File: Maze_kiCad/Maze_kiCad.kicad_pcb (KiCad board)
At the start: 2 copper layers, 1 part, among them U1 ESP32-S2-DevKitC-1

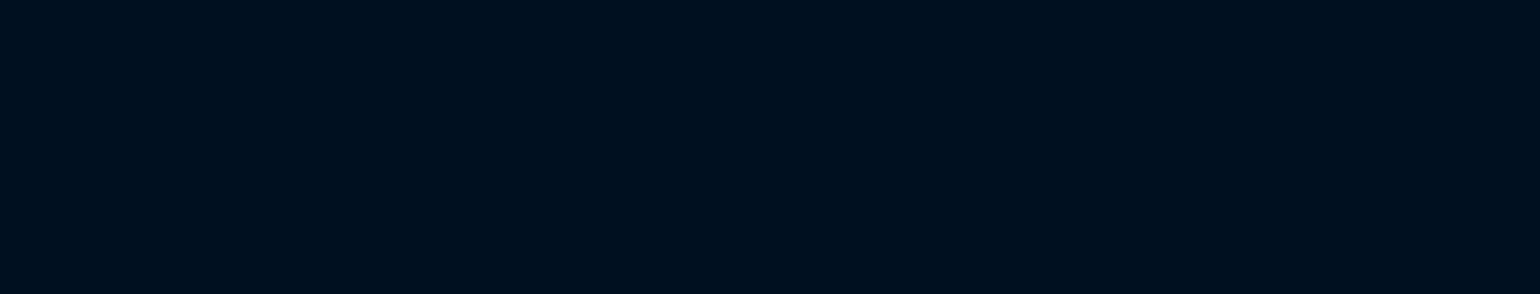
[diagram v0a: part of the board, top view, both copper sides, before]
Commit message: Add ir sensor
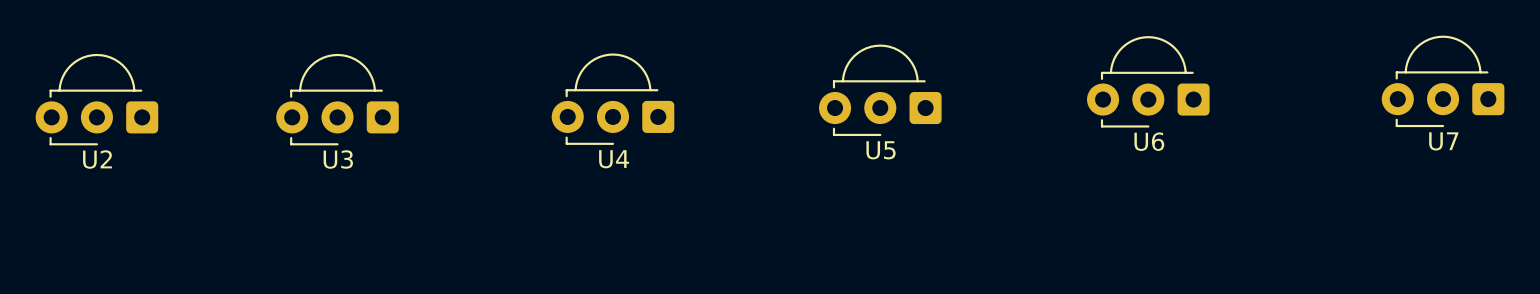
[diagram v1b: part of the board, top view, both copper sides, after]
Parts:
- added U2: TSSP58038, OptoDevice:Vishay_MINICAST-3Pin, F.Cu at (105.5, 27.0)
- added U3: TSSP58038, OptoDevice:Vishay_MINICAST-3Pin, F.Cu at (119.0, 27.0)
- added U4: TSSP58038, OptoDevice:Vishay_MINICAST-3Pin, F.Cu at (134.5, 27.0)
- added U5: TSSP58038, OptoDevice:Vishay_MINICAST-3Pin, F.Cu at (149.5, 26.5)
- added U6: TSSP58038, OptoDevice:Vishay_MINICAST-3Pin, F.Cu at (164.5, 26.0)
- added U7: TSSP58038, OptoDevice:Vishay_MINICAST-3Pin, F.Cu at (181.1, 26.0)

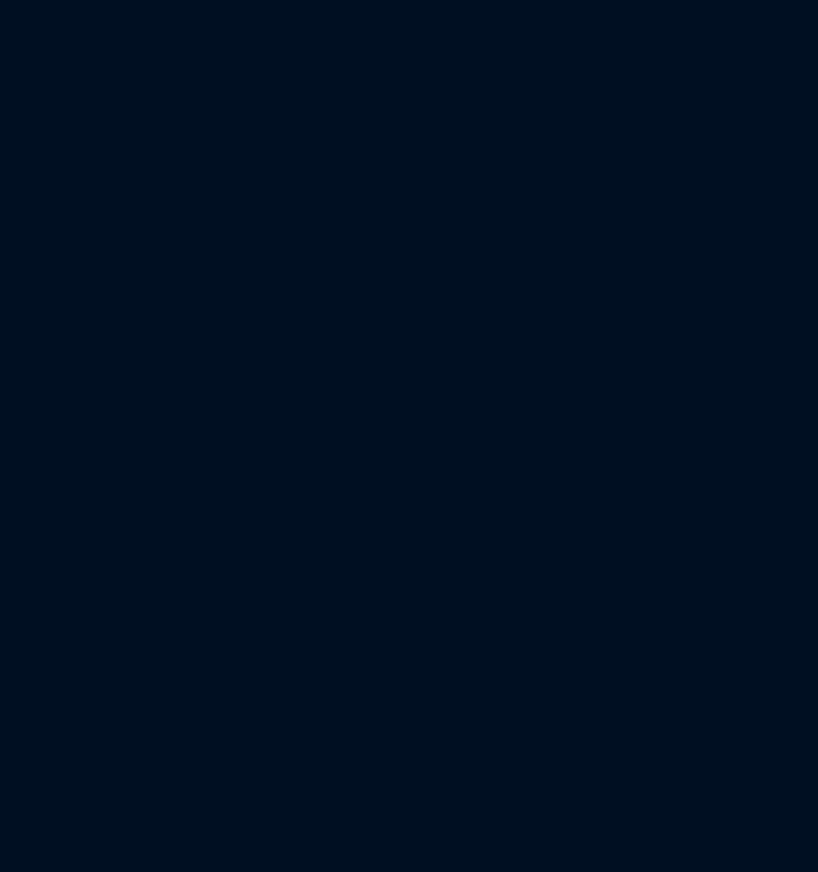
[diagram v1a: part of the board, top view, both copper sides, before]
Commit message: add gyroscope symbol-footprint
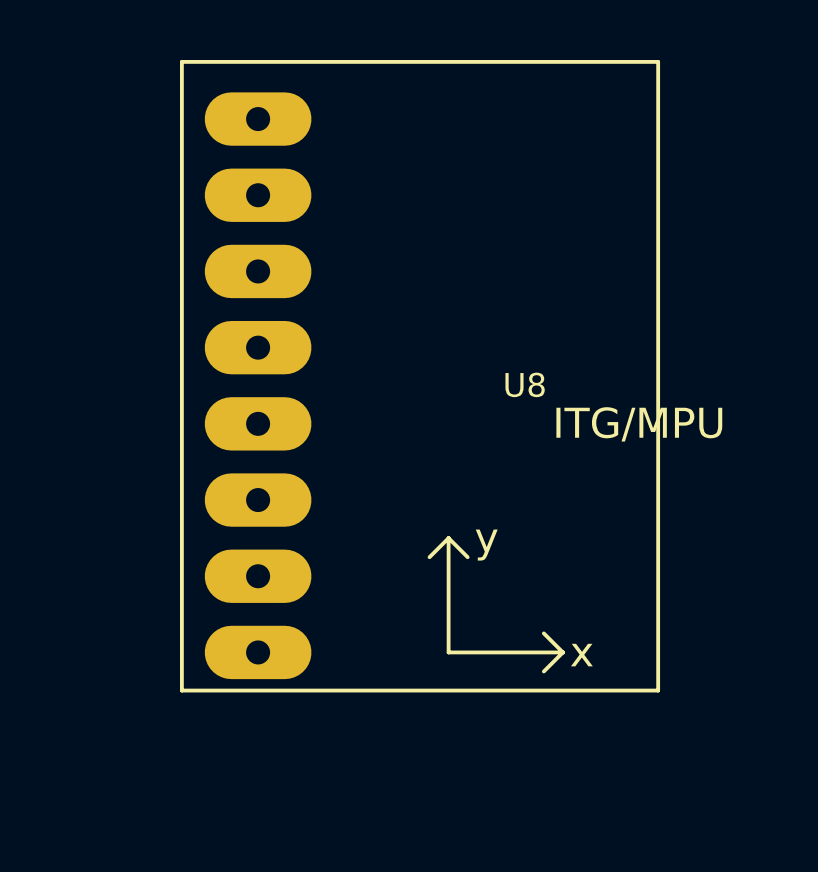
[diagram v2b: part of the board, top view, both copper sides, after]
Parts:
- added U8: GY-521, mpu6050:GY-521, F.Cu at (226.0, 30.5)

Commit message: drv8835 motor driver symnol and footprint
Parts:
- added MotorDriver1: DRV8835, drv8835:drv8835, F.Cu at (75.0, 35.0)

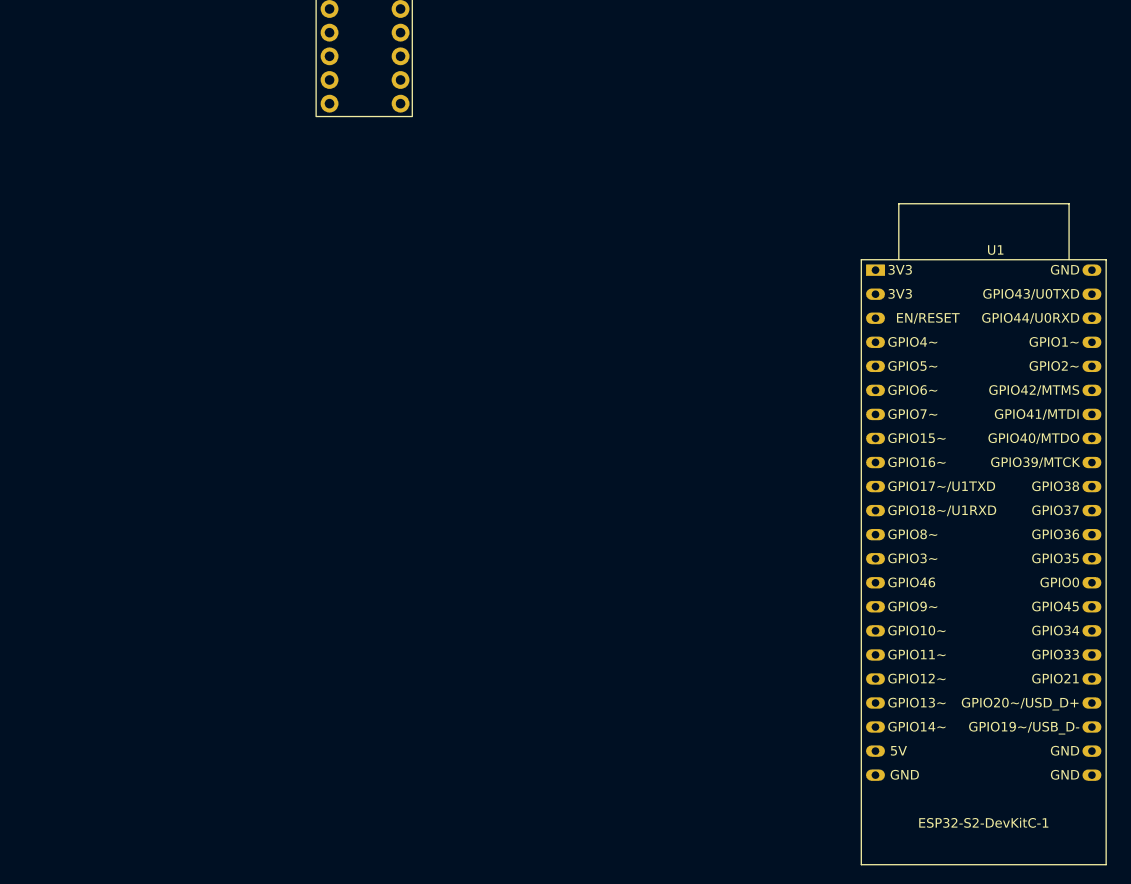
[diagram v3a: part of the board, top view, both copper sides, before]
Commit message: add ultra sonic symbol and footprint
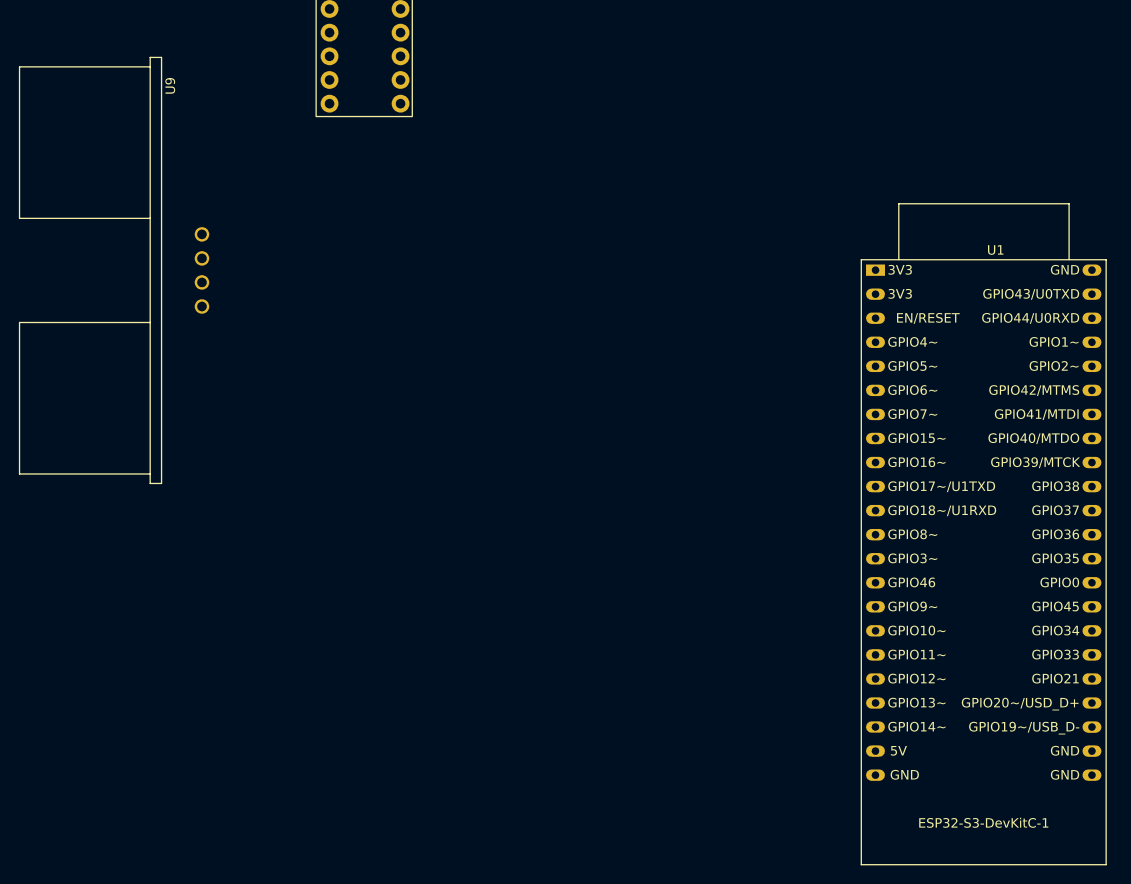
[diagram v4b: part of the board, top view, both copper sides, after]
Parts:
- added U9: HC-SR04, ultrasonic:XCVR_HC-SR04, F.Cu at (58.0, 60.2)
- U1: value ESP32-S2-DevKitC-1 -> ESP32-S3-DevKitC-1
- U2, U3, U4, U5, U6, U7: value TSSP58038 -> TCRT5000
- U8: value GY-521 -> Gyro mpu-6050

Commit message: assign footprints
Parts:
- added D1: RGB, LED_THT:LED_D5.0mm-4_RGB_Staggered_Pins, F.Cu at (112.1, 148.7)
- added D2: RGB, LED_THT:LED_D5.0mm-4_RGB_Staggered_Pins, F.Cu at (112.2, 164.5)
- added J1: Screw_Terminal, TerminalBlock_Phoenix:TerminalBlock_Phoenix_MPT-0,5-2-2.54_1x02_P2.54mm_Horizontal, F.Cu at (109.0, 123.0)
- added J10: pins: 42_41_40_39_38_37, Connector_PinSocket_2.54mm:PinSocket_1x06_P2.54mm_Vertical, F.Cu at (80.0, 100.3)
- added J11: pins: 42_41_40_39_38_37, Connector_PinSocket_2.54mm:PinSocket_1x06_P2.54mm_Vertical, F.Cu at (89.5, 116.2)
- added J12: Vcc/Gnd, Connector_PinSocket_2.54mm:PinSocket_1x04_P2.54mm_Vertical, F.Cu at (131.4, 153.0)
- added J2: motor2, Connector_PinSocket_2.54mm:PinSocket_1x02_P2.54mm_Vertical, F.Cu at (93.0, 93.5)
- added J3: motor1, Connector_PinSocket_2.54mm:PinSocket_1x02_P2.54mm_Vertical, F.Cu at (93.5, 82.8)
- added J4: Vmm/Mode, Connector_PinSocket_2.54mm:PinSocket_1x02_P2.54mm_Vertical, F.Cu at (105.5, 68.0)
- added J5: INT/ADO/XCL/XDA, Connector_PinSocket_2.54mm:PinSocket_1x04_P2.54mm_Vertical, F.Cu at (25.0, 47.0)
- added J6: GND, Connector_PinSocket_2.54mm:PinSocket_1x01_P2.54mm_Vertical, F.Cu at (212.0, 41.5)
- added J7: IR Receiver, Connector_PinSocket_2.54mm:PinSocket_1x03_P2.54mm_Vertical, F.Cu at (121.5, 86.5)
- added J8: pins: 5v/12_11_10_9_46, Connector_PinSocket_2.54mm:PinSocket_1x06_P2.54mm_Vertical, F.Cu at (24.0, 137.0)
- added J9: pins: 3.3v/RST/43_44_2, Connector_PinSocket_2.54mm:PinSocket_1x06_P2.54mm_Vertical, F.Cu at (42.5, 66.5)
- added R1: 220-ohm, Resistor_THT:R_Axial_DIN0204_L3.6mm_D1.6mm_P7.62mm_Horizontal, F.Cu at (84.2, 139.0)
- added R2: 220-ohm, Resistor_THT:R_Axial_DIN0204_L3.6mm_D1.6mm_P7.62mm_Horizontal, F.Cu at (93.7, 150.5)
- added R3: 220-ohm, Resistor_THT:R_Axial_DIN0204_L3.6mm_D1.6mm_P7.62mm_Horizontal, F.Cu at (92.2, 158.0)
- added R4: 220-ohm, Resistor_THT:R_Axial_DIN0204_L3.6mm_D1.6mm_P7.62mm_Horizontal, F.Cu at (96.9, 168.0)
- added R5: 220-ohm, Resistor_THT:R_Axial_DIN0204_L3.6mm_D1.6mm_P7.62mm_Horizontal, F.Cu at (62.9, 163.5)
- added R6: 220-ohm, Resistor_THT:R_Axial_DIN0204_L3.6mm_D1.6mm_P7.62mm_Horizontal, F.Cu at (90.7, 187.0)
- added S1: RB141C1100, RB141C1100:SW_RB141C1100, F.Cu at (134.0, 119.0)
- added U10: Reg S7V7F5, Connector_PinSocket_2.54mm:PinSocket_1x03_P2.54mm_Vertical, F.Cu at (104.4, 107.5)
- moved U8 182.2 mm to (44.0, 38.5)
- moved U9 145.3 mm to (202.0, 40.9), turned to 180 degrees
- moved U1 95.1 mm to (38.6, 89.3)
- moved U7 71.1 mm to (110.0, 23.5)
- moved MotorDriver1 60.0 mm to (106.5, 86.1), turned to 180 degrees
- moved U2 40.2 mm to (145.5, 23.5)
- moved U5 22.2 mm to (171.5, 23.5)
- moved U3 15.4 mm to (134.0, 23.5)
- moved U4 13.5 mm to (121.5, 23.5)
- moved U6 6.50 mm to (158.5, 23.5)
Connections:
- U1 pad 1: unconnected-(U1-3V3-Pad1) -> Net-(J9-Pin_3)
- U1 pad 10: unconnected-(U1-GPIO17/ADC2_CH6/U1TXD-Pad10) -> /ir_sensor_4
- U1 pad 11: unconnected-(U1-GPIO18/ADC2_CH7/U1RXD-Pad11) -> /ir_sensor_3
- U1 pad 12: unconnected-(U1-GPIO8/ADC1_CH7-Pad12) -> /ir_sensor_2
- U1 pad 13: unconnected-(U1-GPIO3/ADC1_CH2-Pad13) -> /ir_sensor_1
- U1 pad 14: unconnected-(U1-GPIO46-Pad14) -> Net-(J8-Pin_6)
- U1 pad 15: unconnected-(U1-GPIO9/ADC1_CH8-Pad15) -> Net-(J8-Pin_5)
- U1 pad 16: unconnected-(U1-GPIO10/ADC1_CH9-Pad16) -> Net-(J8-Pin_4)
- U1 pad 17: unconnected-(U1-GPIO11/ADC2_CH0-Pad17) -> Net-(J8-Pin_3)
- U1 pad 18: unconnected-(U1-GPIO12/ADC2_CH1-Pad18) -> Net-(J8-Pin_2)
- U1 pad 19: unconnected-(U1-GPIO13/ADC2_CH2-Pad19) -> /sda_pin13
- U1 pad 2: unconnected-(U1-3V3-Pad2) -> Net-(J9-Pin_2)
- U1 pad 20: unconnected-(U1-GPIO14/ADC2_CH3-Pad20) -> /scl_pin14
- U1 pad 21: unconnected-(U1-5V-Pad21) -> VCC
- U1 pad 22: unconnected-(U1-GND-Pad22) -> GND
- U1 pad 23: unconnected-(U1-GND-Pad23) -> GND
- U1 pad 24: unconnected-(U1-GND-Pad24) -> GND
- U1 pad 25: unconnected-(U1-GPIO19/ADC2_CH8/USB_D--Pad25) -> /echo_pin19
- U1 pad 26: unconnected-(U1-GPIO20/ADC2_CH9/USB_D+-Pad26) -> /trig_pin20
- U1 pad 27: unconnected-(U1-GPIO21-Pad27) -> /pin21_red
- U1 pad 28: unconnected-(U1-GPIO33-Pad28) -> /pin47_green
- U1 pad 29: unconnected-(U1-GPIO34-Pad29) -> /pin48_blue
- U1 pad 3: unconnected-(U1-RST-Pad3) -> Net-(J9-Pin_1)
- U1 pad 30: unconnected-(U1-GPIO45-Pad30) -> Net-(J11-Pin_4)
- U1 pad 31: unconnected-(U1-GPIO0-Pad31) -> Net-(J11-Pin_3)
- U1 pad 32: unconnected-(U1-GPIO35-Pad32) -> Net-(J11-Pin_2)
- U1 pad 33: unconnected-(U1-GPIO36-Pad33) -> Net-(J11-Pin_1)
- U1 pad 34: unconnected-(U1-GPIO37-Pad34) -> Net-(J10-Pin_6)
- U1 pad 35: unconnected-(U1-GPIO38-Pad35) -> Net-(J10-Pin_5)
- U1 pad 36: unconnected-(U1-GPIO39/MTCK-Pad36) -> Net-(J10-Pin_4)
- U1 pad 37: unconnected-(U1-GPIO40/MTDO-Pad37) -> Net-(J10-Pin_3)
- U1 pad 38: unconnected-(U1-GPIO41/MTDI-Pad38) -> Net-(J10-Pin_2)
- U1 pad 39: unconnected-(U1-GPIO42/MTMS-Pad39) -> Net-(J10-Pin_1)
- U1 pad 4: unconnected-(U1-GPIO4/ADC1_CH3-Pad4) -> /aIn_pin4
- U1 pad 40: unconnected-(U1-GPIO2/ADC1_CH1-Pad40) -> Net-(J9-Pin_6)
- U1 pad 41: unconnected-(U1-GPIO1/ADC1_CH0-Pad41) -> /ir_receiver_pin1
- U1 pad 42: unconnected-(U1-GPIO44/U0RXD-Pad42) -> Net-(J9-Pin_5)
- U1 pad 43: unconnected-(U1-GPIO43/U0TXD-Pad43) -> Net-(J9-Pin_4)
- U1 pad 44: unconnected-(U1-GND-Pad44) -> GND
- U1 pad 5: unconnected-(U1-GPIO5/ADC1_CH4-Pad5) -> /aEnb_pin5
- U1 pad 6: unconnected-(U1-GPIO6/ADC1_CH5-Pad6) -> /bIn_pin6
- U1 pad 7: unconnected-(U1-GPIO7/ADC1_CH6-Pad7) -> /bEnb_pin7
- U1 pad 8: unconnected-(U1-GPIO15/ADC2_CH4/32K_P-Pad8) -> /ir_sensor_6
- U1 pad 9: unconnected-(U1-GPIO16/ADC2_CH5/32K_N-Pad9) -> /ir_sensor_5
- U2 pad 1: unconnected-(U2-VCC-Pad1) -> VCC
- U2 pad 2: unconnected-(U2-OUT-Pad2) -> /ir_sensor_1
- U2 pad 3: unconnected-(U2-GND-Pad3) -> GND
- U3 pad 1: unconnected-(U3-VCC-Pad1) -> VCC
- U3 pad 2: unconnected-(U3-OUT-Pad2) -> /ir_sensor_2
- U3 pad 3: unconnected-(U3-GND-Pad3) -> GND
- U4 pad 1: unconnected-(U4-VCC-Pad1) -> VCC
- U4 pad 2: unconnected-(U4-OUT-Pad2) -> /ir_sensor_3
- U4 pad 3: unconnected-(U4-GND-Pad3) -> GND
- U5 pad 1: unconnected-(U5-VCC-Pad1) -> VCC
- U5 pad 2: unconnected-(U5-OUT-Pad2) -> /ir_sensor_4
- U5 pad 3: unconnected-(U5-GND-Pad3) -> GND
- U6 pad 1: unconnected-(U6-VCC-Pad1) -> VCC
- U6 pad 2: unconnected-(U6-OUT-Pad2) -> /ir_sensor_5
- U6 pad 3: unconnected-(U6-GND-Pad3) -> GND
- U7 pad 1: unconnected-(U7-VCC-Pad1) -> VCC
- U7 pad 2: unconnected-(U7-OUT-Pad2) -> /ir_sensor_6
- U7 pad 3: unconnected-(U7-GND-Pad3) -> GND
- U8 pad ADO: unconnected-(U8-PadADO) -> Net-(J5-Pin_2)
- U8 pad GND: unconnected-(U8-PadGND) -> GND
- U8 pad INT: unconnected-(U8-PadINT) -> Net-(J5-Pin_1)
- U8 pad SCL: unconnected-(U8-PadSCL) -> /scl_pin14
- U8 pad SDA: unconnected-(U8-PadSDA) -> /sda_pin13
- U8 pad VCC: unconnected-(U8-PadVCC) -> VCC
- U8 pad XCL: unconnected-(U8-PadXCL) -> Net-(J5-Pin_3)
- U8 pad XDA: unconnected-(U8-PadXDA) -> Net-(J5-Pin_4)
- U9 pad 1: unconnected-(U9-VCC-Pad1) -> VCC
- U9 pad 2: unconnected-(U9-TRIG-Pad2) -> /trig_pin20
- U9 pad 3: unconnected-(U9-ECHO-Pad3) -> /echo_pin19

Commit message: Remove the resistors because the two LEDs use the same pins
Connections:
- D2 pad 1: Net-(D2-RA) -> Net-(D1-RA)
- D2 pad 2: Net-(D2-GA) -> Net-(D1-GA)
- D2 pad 3: Net-(D2-BA) -> Net-(D1-BA)
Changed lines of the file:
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@@
 			(remove_unused_layers no)
 			(roundrect_rratio 0.25)
-			(net 6 "Net-(D2-RA)")
+			(net 2 "Net-(D1-RA)")
 			(pinfunction "RA")
 			(pintype "passive")
@@
 			(layers "*.Cu" "*.Mask")
 			(remove_unused_layers no)
-			(net 5 "Net-(D2-GA)")
+			(net 1 "Net-(D1-GA)")
 			(pinfunction "GA")
 			(pintype "passive")
@@
 			(layers "*.Cu" "*.Mask")
 			(remove_unused_layers no)
-			(net 7 "Net-(D2-BA)")
+			(net 3 "Net-(D1-BA)")
 			(pinfunction "BA")
 			(pintype "passive")
